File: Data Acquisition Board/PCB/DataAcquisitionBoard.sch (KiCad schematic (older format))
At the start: 14 parts, among them P1 BNC, P2 BNC, P3 BNC, P4 BNC, P5 CONN_01X04

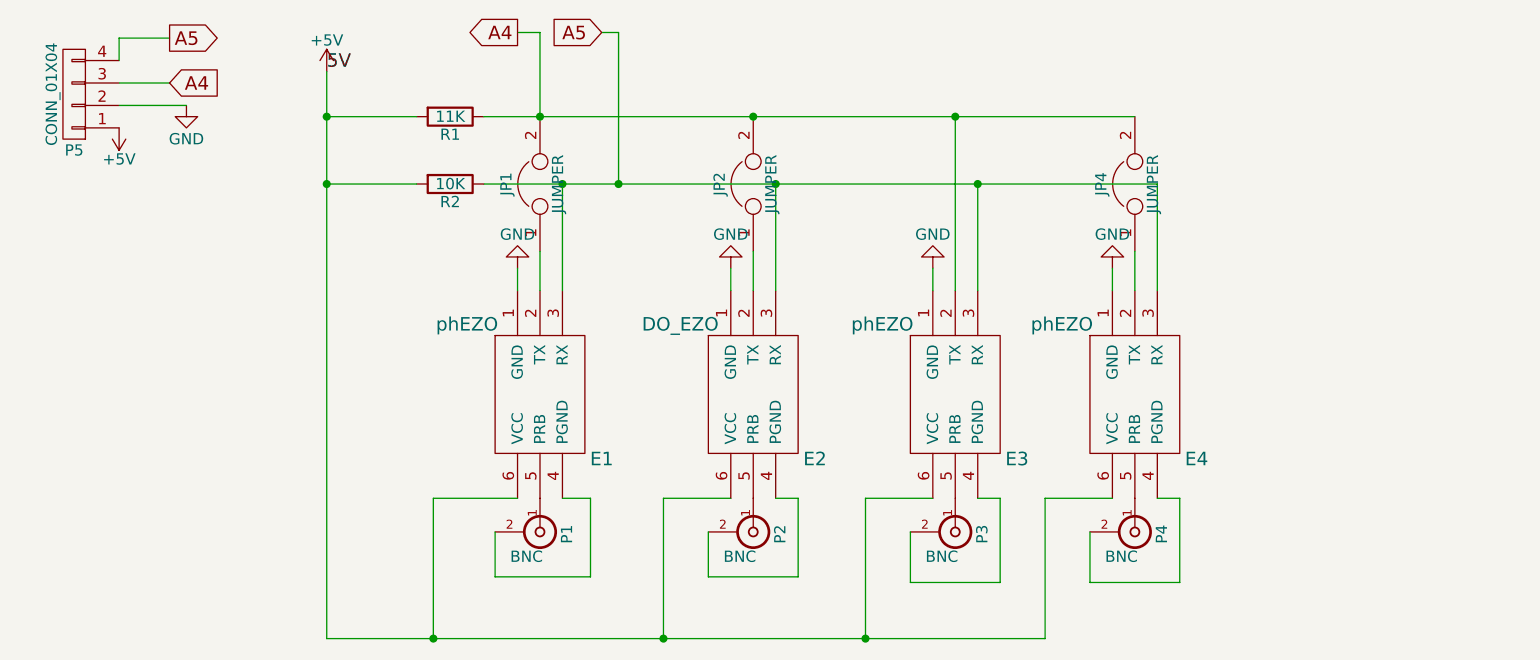
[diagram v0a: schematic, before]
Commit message: Updated PCB to allow for chaining of multiple boards
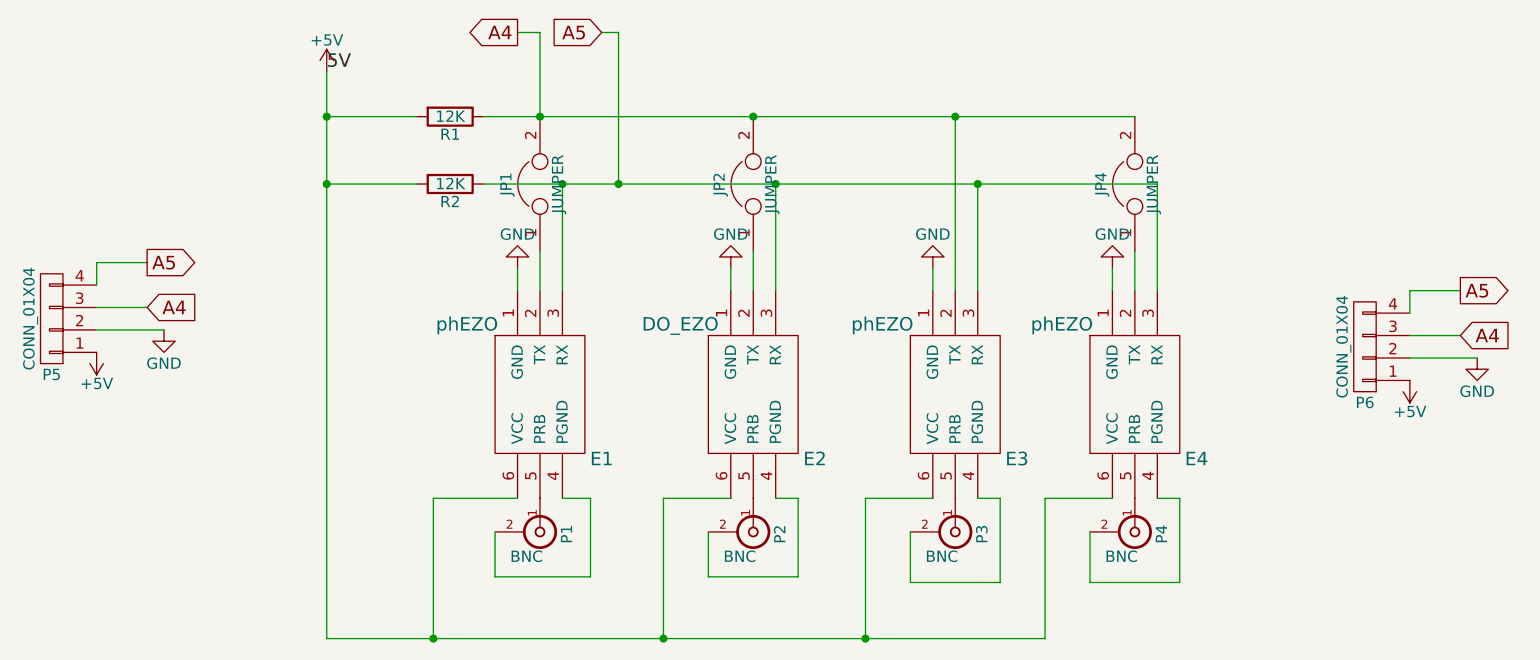
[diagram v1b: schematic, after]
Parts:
- added P6: CONN_01X04, Pin_Headers:Pin_Header_Straight_1x04_Pitch2.54mm, symbol CONN_01X04
- P5: footprint Pin_Headers:Pin_Header_Straight_1x04 -> Pin_Headers:Pin_Header_Straight_1x04_Pitch2.54mm
- R1: value 11K -> 12K
- R2: value 10K -> 12K
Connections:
- net +5V: now also P6.1 (P1)
- net A4: now also P6.3 (P3)
- net A5: now also P6.4 (P4)
- net GND: now also P6.2 (P2)
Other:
- moved on the sheet: P5
